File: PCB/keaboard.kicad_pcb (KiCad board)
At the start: 2 copper layers, 75 parts, among them U1 ProMicro

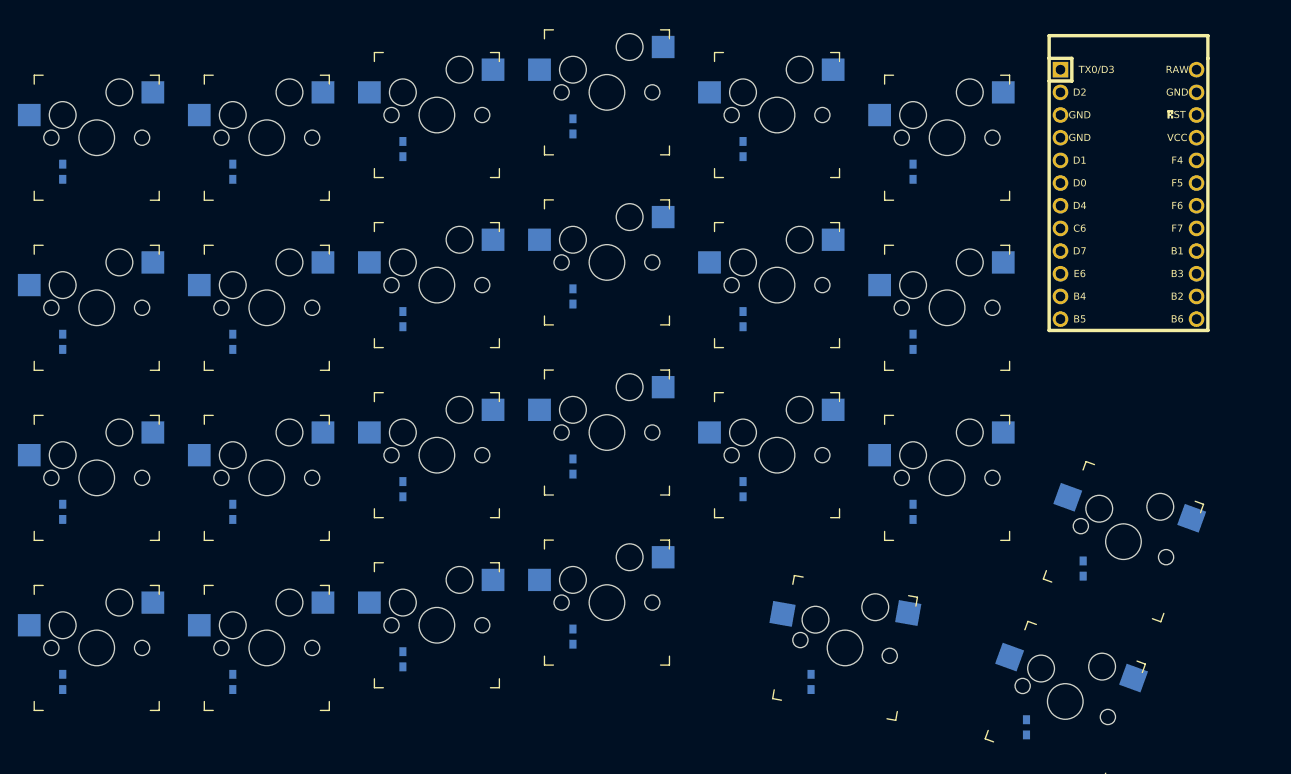
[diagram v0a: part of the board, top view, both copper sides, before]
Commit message: Add traces, add TRRS jack, add B+/B- pins, update README
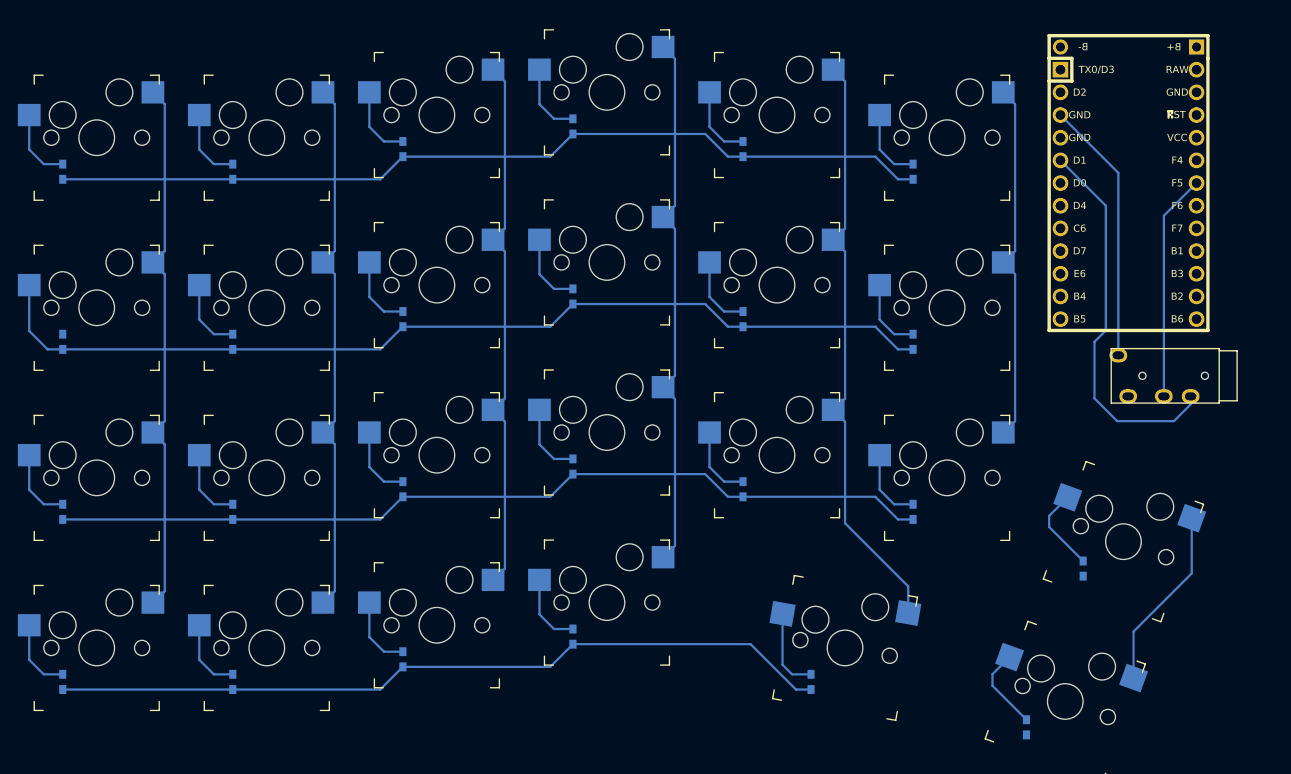
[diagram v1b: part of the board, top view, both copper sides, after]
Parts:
- added P?: CONN_1, keyboard_parts:PIN_1_SQUARE, F.Cu at (174.0, 34.3)
- added P?: CONN_1, keyboard_parts:PIN_1, F.Cu at (158.8, 34.3)
- added REF**: TRRS-PJ-320A, Keebio-Parts:TRRS-PJ-320A, F.Cu at (176.5, 71.1)
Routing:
- net (no net): track 0.00 -> 1066.3 mm
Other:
- board text added: "B+"
- board text added: "B-"

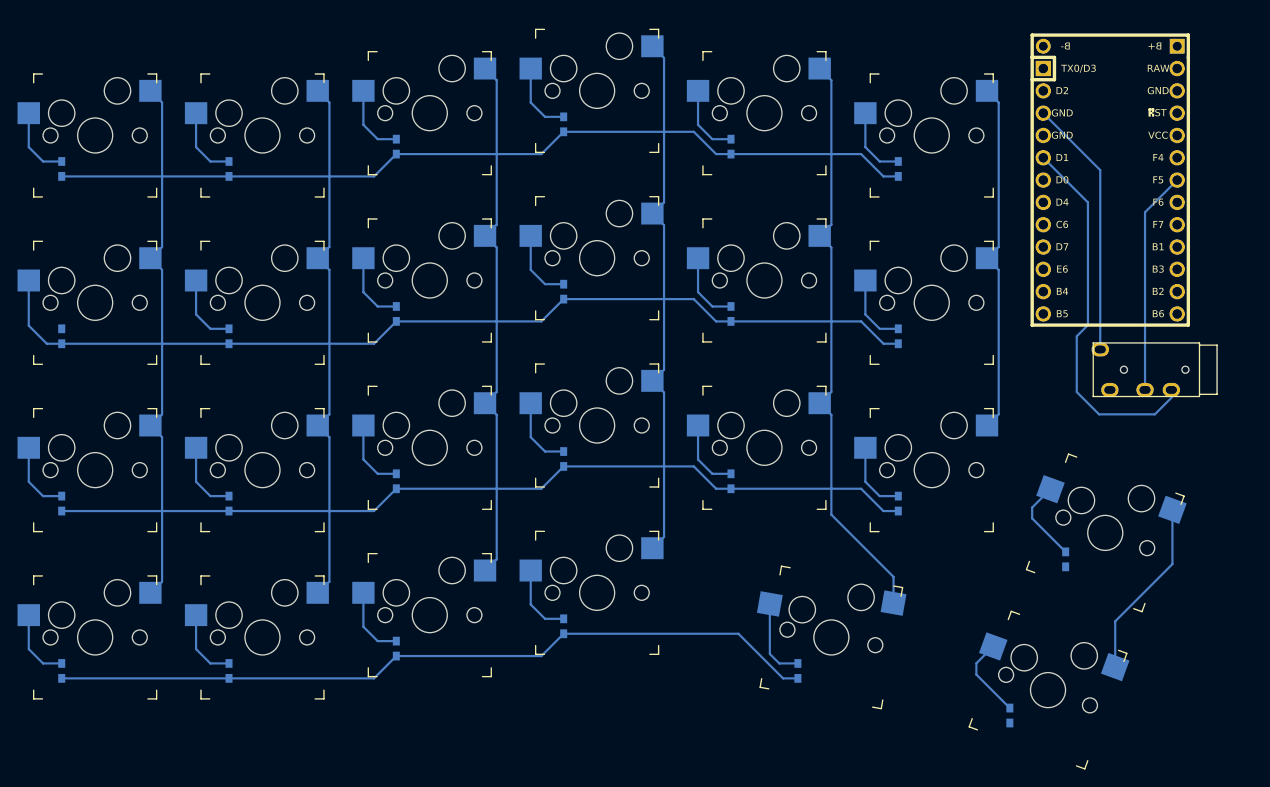
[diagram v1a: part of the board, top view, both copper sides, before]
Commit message: Connect matrix to data pins
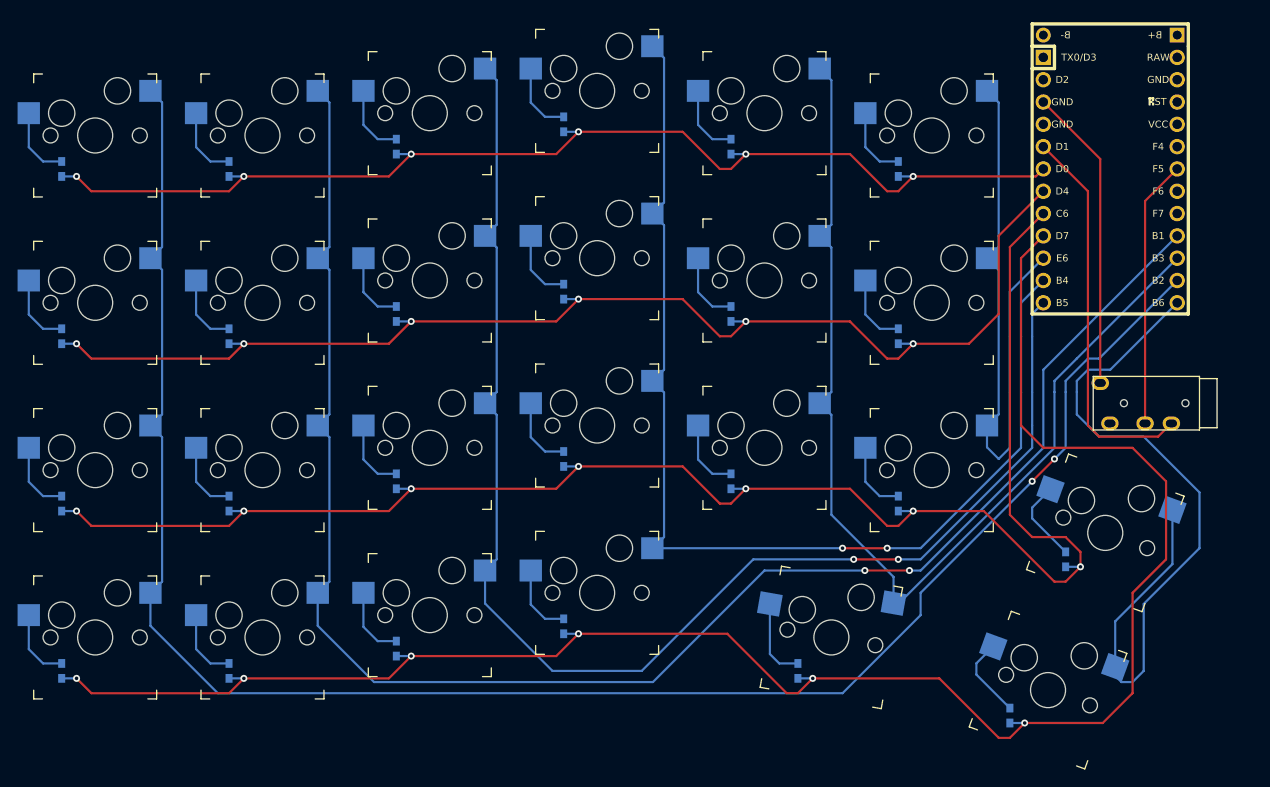
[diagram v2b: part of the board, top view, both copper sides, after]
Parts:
- moved REF** 3.81 mm to (176.5, 74.9)
- moved P? 1.27 mm to (174.0, 33.0)
- moved P? 1.27 mm to (158.8, 33.0)
- moved U1 1.27 mm to (166.4, 49.5)
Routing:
- net (no net): track 1066.3 -> 1946.3 mm, vias 0 -> 33

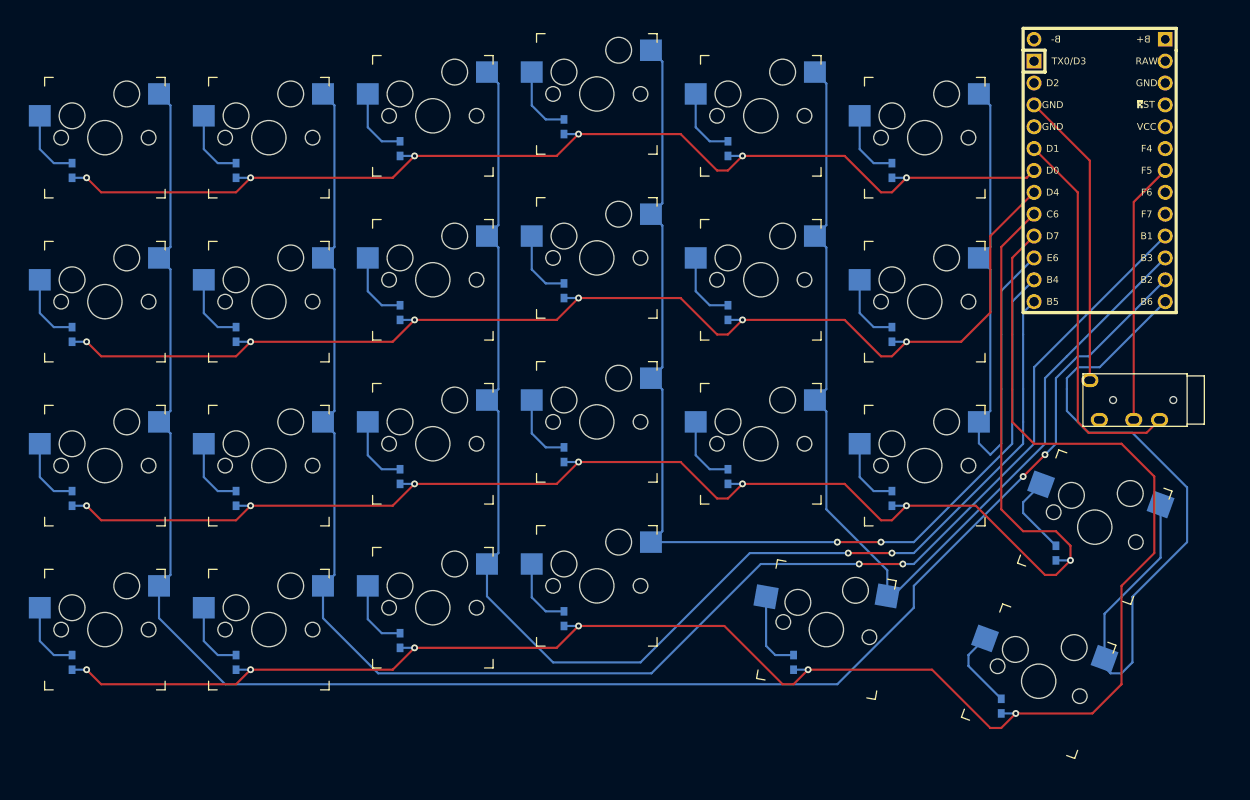
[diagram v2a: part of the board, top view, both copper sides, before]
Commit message: Minor rerouting, add reset switch, add edge cut
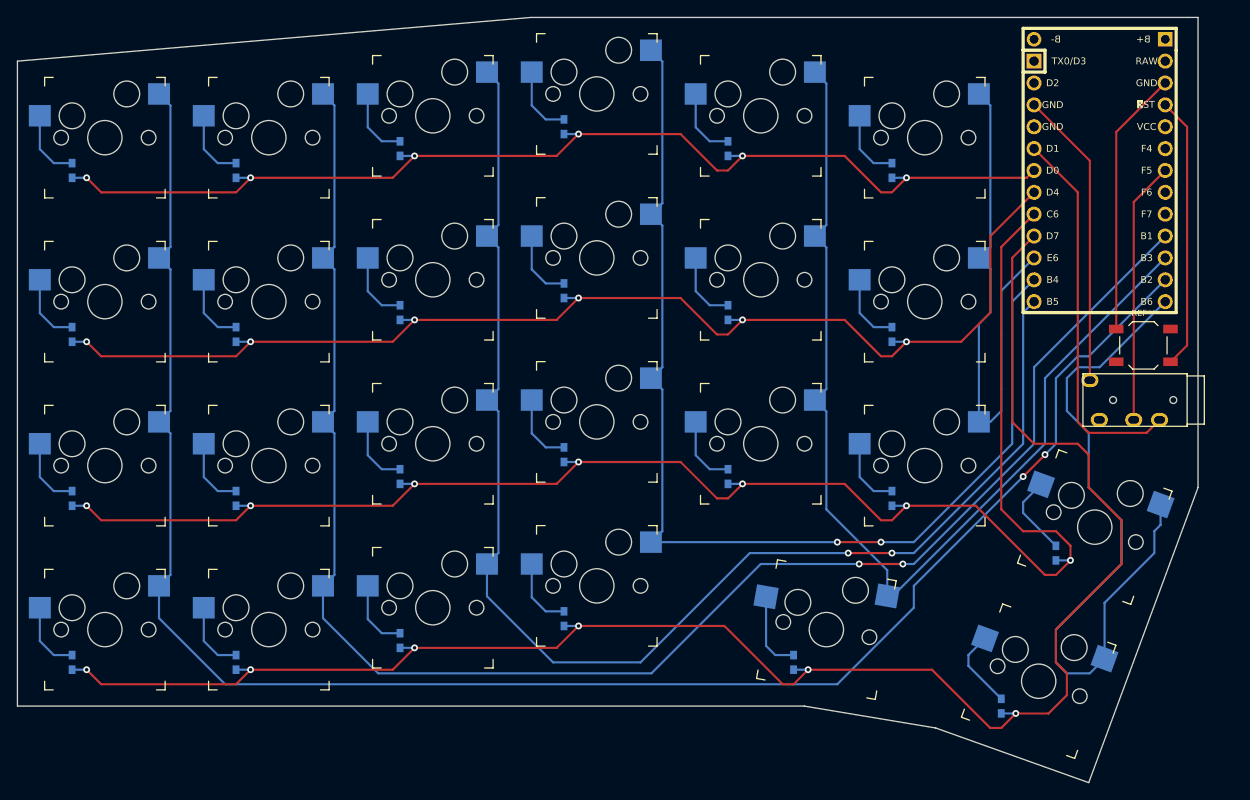
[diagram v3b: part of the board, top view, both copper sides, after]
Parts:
- added REF**: SW_SPST_TL3342, Keebio-Parts:SW_SPST_TL3342, F.Cu at (171.4, 68.6)
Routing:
- net (no net): track 1946.3 -> 1990.2 mm
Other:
- board outline added: 137.2 x 88.9 mm

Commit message: Add keaboard label
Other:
- board text added: "keaboard rev1"

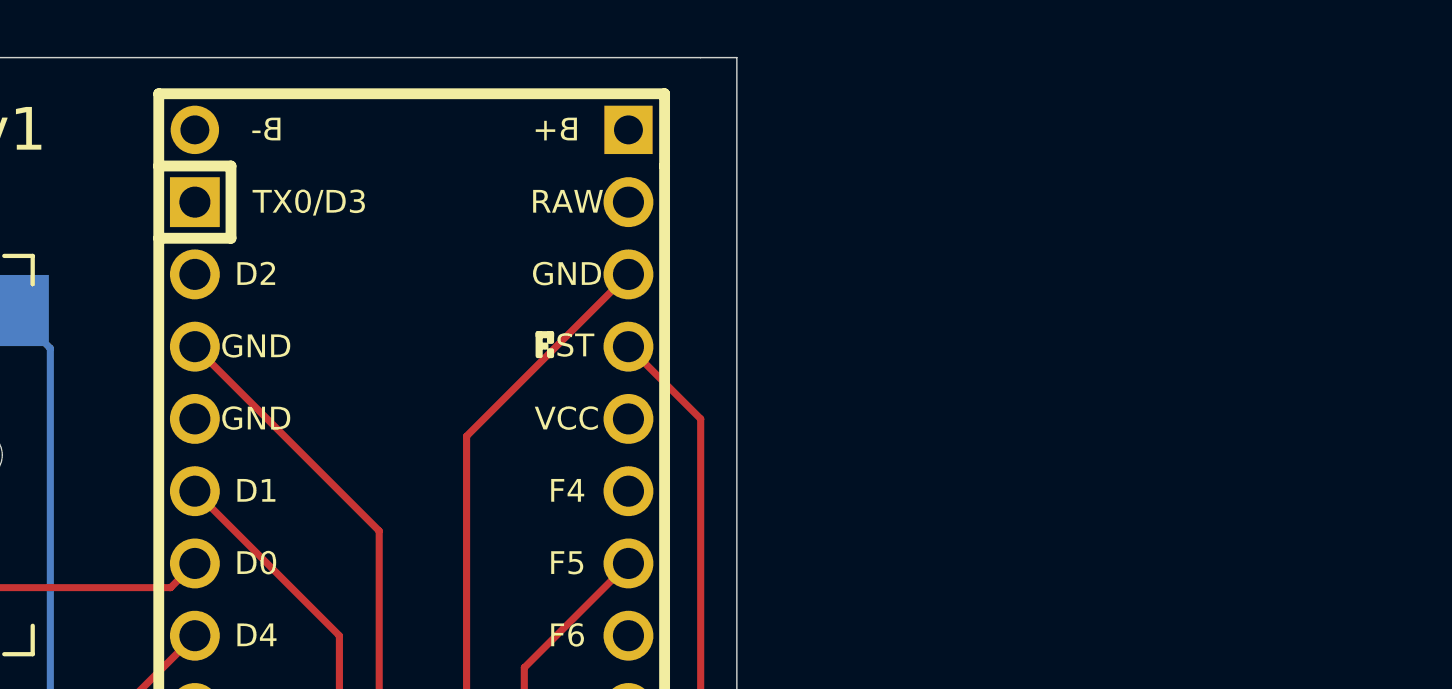
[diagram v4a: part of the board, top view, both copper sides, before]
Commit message: Add 3-pin JST connector, remove B+/B- pin holes
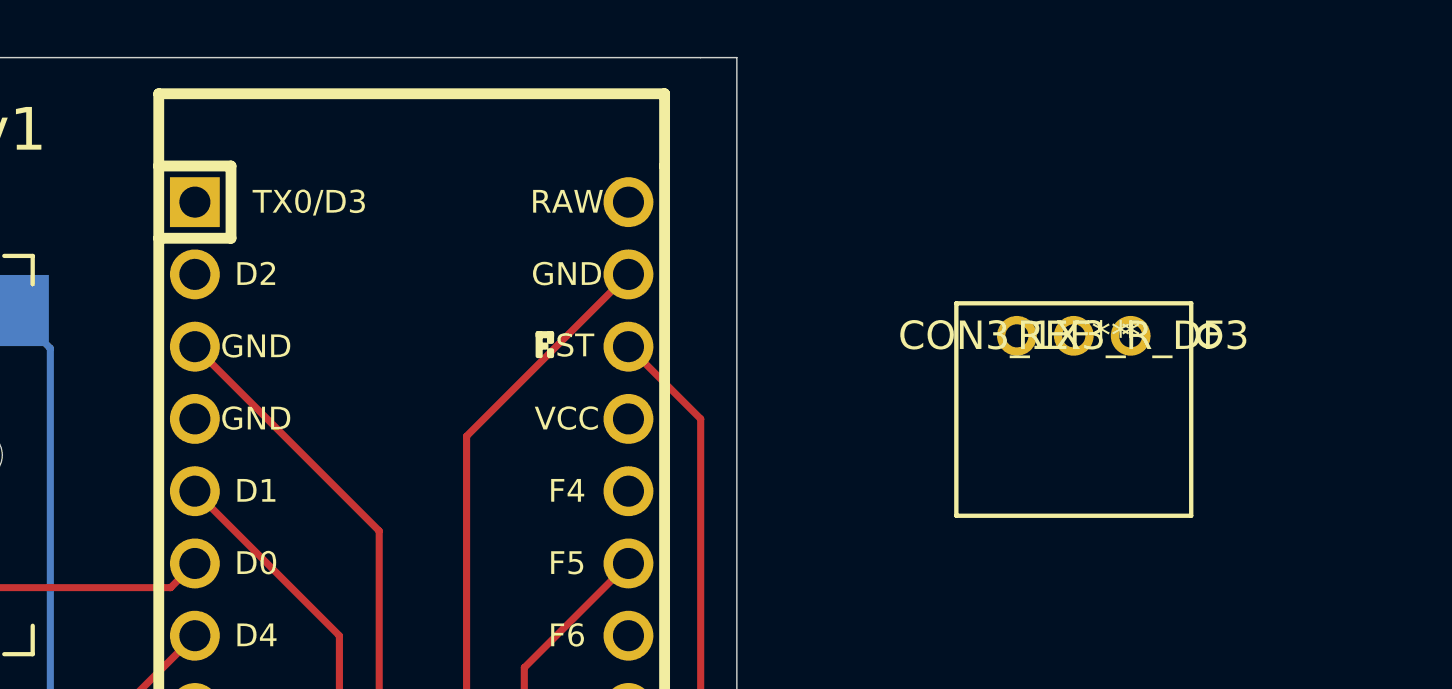
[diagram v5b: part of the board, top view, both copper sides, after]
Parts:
- removed P?: CONN_1, keyboard_parts:PIN_1_SQUARE
- removed P?: CONN_1, keyboard_parts:PIN_1
- added REF**: CON3_1X3_R_DF3, parts:DF3A-3P-2DS, F.Cu at (191.6, 40.3)
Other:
- board text removed: "B+"
- board text removed: "B-"
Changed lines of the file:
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@@
   (general
     (thickness 1.6)
-    (drawings 14)
+    (drawings 10)
     (tracks 385)
     (zones 0)
-    (modules 79)
+    (modules 78)
     (nets 1)
   )
@@
     (uvia_drill 0.1)
   )
+  (module parts:DF3A-3P-2DS (layer F.Cu)
+    (at 191.643 40.259)
+    (fp_text reference REF** (at -2 0) (layer F.SilkS)
+      (effects (font (size 1 1) (thickness 0.15)))
+    )
+    (fp_text value CON3_1X3_R_DF3 (at -2 0) (layer F.SilkS)
+      (effects (font (size 1 1) (thickness 0.15)))
+    )
+    (fp_text user * (at 0 0) (layer F.Fab)
+      (effects (font (size 1 1) (thickness 0.15)))
+    )
+    (fp_text user * (at 0 0) (layer F.SilkS)
+      (effects (font (size 1 1) (thickness 0.15)))
+    )
+    (fp_text user "Copyright 2016 Accelerated Designs. All rights reserved." (at 0 0) (layer Cmts.User)
+      (effects (font (size 0.127 0.127) (thickness 0.002)))
+    )
+    (fp_line (start -6.1275 6.3246) (end 2.1275 6.3246) (layer F.SilkS) (width 0.1524))
+    (fp_line (start 2.1275 6.3246) (end 2.1275 -1.143) (layer F.SilkS) (width 0.1524))
+    (fp_line (start 2.1275 -1.143) (end -6.1275 -1.143) (layer F.SilkS) (width 0.1524))
+    (fp_line (start -6.1275 -1.143) (end -6.1275 6.3246) (layer F.SilkS) (width 0.1524))
+    (fp_line (start -6.0005 6.1976) (end 2.0005 6.1976) (layer F.Fab) (width 0.1524))
+    (fp_line (start 2.0005 6.1976) (end 2.0005 -1.016) (layer F.Fab) (width 0.1524))
+    (fp_line (start 2.0005 -1.016) (end -6.0005 -1.016) (layer F.Fab) (width 0.1524))
+    (fp_line (start -6.0005 -1.016) (end -6.0005 6.1976) (layer F.Fab) (width 0.1524))
+    (fp_line (start -6.2545 -1.27) (end -6.2545 6.4516) (layer F.CrtYd) (width 0.1524))
+    (fp_line (start -6.2545 6.4516) (end 2.2545 6.4516) (layer F.CrtYd) (width 0.1524))
+    (fp_line (start 2.2545 6.4516) (end 2.2545 -1.27) (layer F.CrtYd) (width 0.1524))
+    (fp_line (start 2.2545 -1.27) (end -6.2545 -1.27) (layer F.CrtYd) (width 0.1524))
+    (fp_line (start -6.0005 -1.016) (end -6.0005 6.1976) (layer F.CrtYd) (width 0.1524))
+    (fp_line (start -6.0005 6.1976) (end 2.0005 6.1976) (layer F.CrtYd) (width 0.1524))
+    (fp_line (start 2.0005 6.1976) (end 2.0005 -1.016) (layer F.CrtYd) (width 0.1524))
+    (fp_line (start 2.0005 -1.016) (end -6.0005 -1.016) (layer F.CrtYd) (width 0.1524))
+    (fp_circle (center 2.7625 0) (end 3.1435 0) (layer F.SilkS) (width 0.1524))
+    (fp_circle (center 2.7625 0) (end 3.1435 0) (layer B.SilkS) (width 0.1524))
+    (fp_circle (center 0 1.905) (end 0.381 1.905) (layer F.Fab) (width 0.1524))
+    (pad 3 thru_hole circle (at -4.000001 0) (size 1.397 1.397) (drill 0.8128) (layers *.Cu *.Mask))
+    (pad 2 thru_hole circle (at -2 0) (size 1.397 1.397) (drill 0.8128) (layers *.Cu *.Mask))
+    (pad 1 thru_hole circle (at 0.000001 0) (size 1.397 1.397) (drill 0.8128) (layers *.Cu *.Mask))
+  )
   (module Keebio-Parts:SW_SPST_TL3342 (layer F.Cu)
     (at 171.45 68.58)
@@
     (pad 2 smd rect (at -7.56 -2.54) (size 2.55 2.5) (layers B.Cu B.Paste B.Mask))
   )
-  (module keyboard_parts:PIN_1_SQUARE (layer F.Cu)
-    (at 173.99 33.02)
-    (tags "CONN pin 1 square")
-    (fp_text reference P? (at 0 -1.55) (layer F.SilkS) hide
-      (effects (font (size 0.8 0.8) (thickness 0.15)))
-    )
-    (fp_text value CONN_1 (at 0 -1.55) (layer F.SilkS) hide
-      (effects (font (size 0.8 0.8) (thickness 0.15)))
-    )
-    (pad 1 thru_hole rect (at 0 0) (size 1.7 1.7) (drill 1.016) (layers *.Cu *.Mask F.SilkS))
-  )
-  (module keyboard_parts:PIN_1 (layer F.Cu)
-    (at 158.75 33.02)
-    (tags "CONN pin 1 circle")
-    (fp_text reference P? (at 0 -1.45) (layer F.SilkS) hide
-      (effects (font (size 0.8 0.8) (thickness 0.15)))
-    )
-    (fp_text value CONN_1 (at 0 -1.45) (layer F.SilkS) hide
-      (effects (font (size 0.8 0.8) (thickness 0.15)))
-    )
-    (pad 1 thru_hole circle (at 0 0) (size 1.7 1.7) (drill 1.016) (layers *.Cu *.Mask F.SilkS))
-  )
   (module keyboard_parts:D_SC79 (layer B.Cu)
     (at 154.94 110.49 90)
@@
   (gr_line (start 100.33 30.48) (end 40.64 35.56) (layer Edge.Cuts) (width 0.05))
   (gr_line (start 176.53 30.48) (end 100.33 30.48) (layer Edge.Cuts) (width 0.05))
-  (gr_text B- (at 161.29 33.02) (layer B.SilkS)
-    (effects (font (size 0.8 0.8) (thickness 0.15)))
-  )
-  (gr_text B- (at 161.29 33.02) (layer F.SilkS)
-    (effects (font (size 0.8 0.8) (thickness 0.15)) (justify mirror))
-  )
-  (gr_text B+ (at 171.45 33.02) (layer F.SilkS)
-    (effects (font (size 0.8 0.8) (thickness 0.15)) (justify mirror))
-  )
-  (gr_text B+ (at 171.45 33.02) (layer B.SilkS)
-    (effects (font (size 0.8 0.8) (thickness 0.15)))
-  )
   (segment (start 152.34 58.42) (end 152.4 58.42) (width 0.25) (layer B.Cu) (net 0))
   (segment (start 152.4 58.42) (end 153.67 57.15) (width 0.25) (layer B.Cu) (net 0))
